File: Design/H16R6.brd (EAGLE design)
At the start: 30 x 34.6 mm, 111 parts, among them IC1 74LVC2T45HK3-7, P1 HEXABIT_17.32, U1 STM32G0B1CEU6N, X1 XTALL_CSTCE8M00G52

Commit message: Edit the logo Add the TVS diode
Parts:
- added D66: BOURNS_CDSOD323-T03SCBOURNS_CDSOD323-T03SC_0_0, HEXABITZ_RCLS:BOURNS_CDSOD323-T03SC_0
- added TRIMBLE-LOGO1: HEXA-LOGO, HEXABITZ_USER_INTERFACE_PARTS:HEXA-LOGO
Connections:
- net GND: now also D66.1
- net VDD: now also D66.2
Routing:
- net GND: track 3.19 -> 4.65 mm
- net VDD: track 23.7 -> 24.2 mm

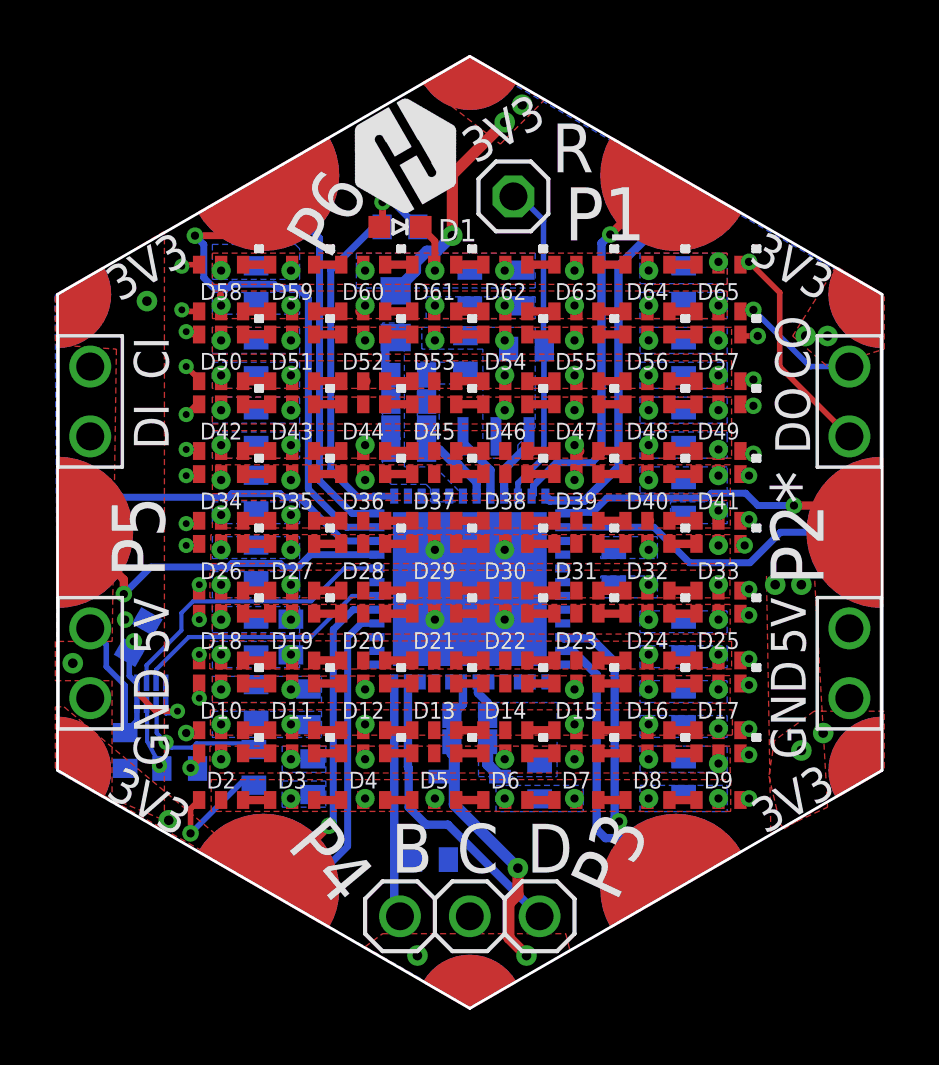
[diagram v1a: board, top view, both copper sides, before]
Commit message: Fix the clearance and soldermask issues Replace the 0603 4.7uF tant cap with ceramic cap in the BOM
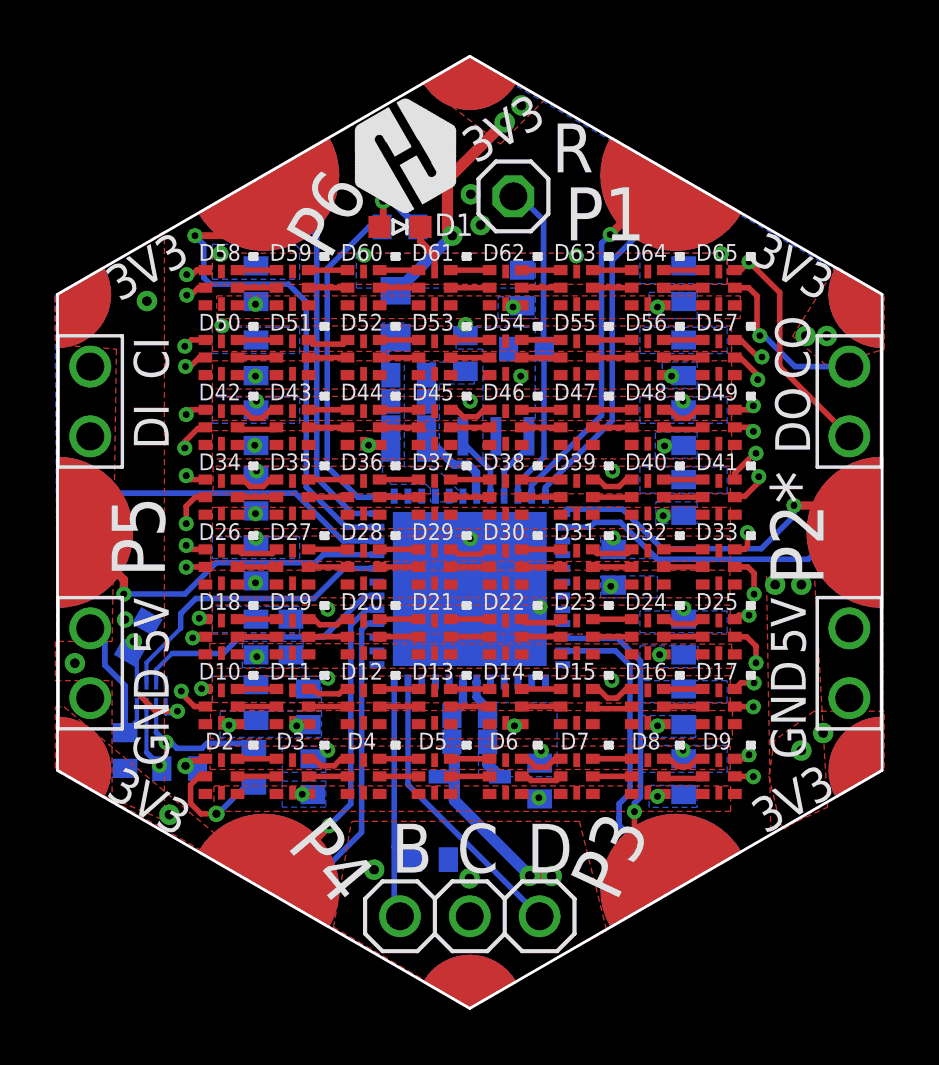
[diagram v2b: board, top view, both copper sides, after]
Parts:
- removed C1: 100nF, HEXABITZ_RCLS:C-0402
- moved SERIAL_IN 27.6 mm to (-13.8, 23.3)
- moved SERIAL_OUT 27.6 mm to (13.8, 23.3)
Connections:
- net +VS: now also D10.VDD1, D11.VDD1, D12.VDD1, D13.VDD1, D14.VDD1, D15.VDD1, D16.VDD1, D17.VDD1, D18.VDD1, D19.VDD1, D2.VDD1, D20.VDD1, D21.VDD1, D22.VDD1, D23.VDD1, D24.VDD1, D25.VDD1, D26.VDD1, D27.VDD1, D28.VDD1, D29.VDD1, D3.VDD1, D30.VDD1, D31.VDD1, D32.VDD1, D33.VDD1, D34.VDD1, D35.VDD1, D36.VDD1, D37.VDD1, D38.VDD1, D39.VDD1, D4.VDD1, D40.VDD1, D41.VDD1, D42.VDD1, D43.VDD1, D44.VDD1, D45.VDD1, D46.VDD1, D47.VDD1, D48.VDD1, D49.VDD1, D5.VDD1, D50.VDD1, D51.VDD1, D52.VDD1, D53.VDD1, D54.VDD1, D55.VDD1, D56.VDD1, D57.VDD1, D58.VDD1, D59.VDD1, D6.VDD1, D60.VDD1, D61.VDD1, D62.VDD1, D63.VDD1, D64.VDD1, D65.VDD1, D7.VDD1, D8.VDD1, D9.VDD1; no longer C1.1
- net CKI: now also SERIAL_IN.1; no longer SERIAL_OUT.1
- net CKO: now also D65.CO, SERIAL_OUT.1; no longer D65.CKO, SERIAL_IN.1
- net GND: no longer C1.2
- net L1_CLK: now also D10.CI, D9.CO; no longer D10.CKI, D9.CKO
- net L1_DATA: now also D10.DI, D9.DO; no longer D10.SDI, D9.SDO
- net L2_CLK: now also D17.CO, D18.CI; no longer D17.CKO, D18.CKI
- net L2_DATA: now also D17.DO, D18.DI; no longer D17.SDO, D18.SDI
- net L3_CLK: now also D25.CO, D26.CI; no longer D25.CKO, D26.CKI
- net L3_DATA: now also D25.DO, D26.DI; no longer D25.SDO, D26.SDI
- net L4_CLK: now also D33.CO, D34.CI; no longer D33.CKO, D34.CKI
- net L4_DATA: now also D33.DO, D34.DI; no longer D33.SDO, D34.SDI
- net L5_CLK: now also D41.CO, D42.CI; no longer D41.CKO, D42.CKI
- net L5_DATA: now also D41.DO, D42.DI; no longer D41.SDO, D42.SDI
- net L6_CLK: now also D49.CO, D50.CI; no longer D49.CKO, D50.CKI
- net L6_DATA: now also D49.DO, D50.DI; no longer D49.SDO, D50.SDI
- net L7_CLK: now also D57.CO, D58.CI; no longer D57.CKO, D58.CKI
- net L7_DATA: now also D57.DO, D58.DI; no longer D57.SDO, D58.SDI
- net N$1: now also D3.DO, D4.DI; no longer D3.SDO, D4.SDI
- net N$10: now also D8.CO, D9.CI; no longer D8.CKO, D9.CKI
- net N$100: now also D45.DO, D46.DI; no longer D45.SDO, D46.SDI
- net N$101: now also D45.CO, D46.CI; no longer D45.CKO, D46.CKI
- net N$102: now also D46.CO, D47.CI; no longer D46.CKO, D47.CKI
- net N$103: now also D46.DO, D47.DI; no longer D46.SDO, D47.SDI
- net N$104: now also D47.CO, D48.CI; no longer D47.CKO, D48.CKI
- net N$105: now also D47.DO, D48.DI; no longer D47.SDO, D48.SDI
- net N$106: now also D12.DO, D13.DI; no longer D12.SDO, D13.SDI
- net N$107: now also D13.DO, D14.DI; no longer D13.SDO, D14.SDI
- net N$108: now also D13.CO, D14.CI; no longer D13.CKO, D14.CKI
- net N$109: now also D14.CO, D15.CI; no longer D14.CKO, D15.CKI
- net N$11: now also D7.CO, D8.CI; no longer D7.CKO, D8.CKI
- net N$110: now also D14.DO, D15.DI; no longer D14.SDO, D15.SDI
- net N$111: now also D15.CO, D16.CI; no longer D15.CKO, D16.CKI
- net N$112: now also D15.DO, D16.DI; no longer D15.SDO, D16.SDI
- net N$113: now also D4.CO, D5.CI; no longer D4.CKO, D5.CKI
- net N$114: now also D4.DO, D5.DI; no longer D4.SDO, D5.SDI
- net N$115: now also D6.CO, D7.CI; no longer D6.CKO, D7.CKI
- net N$116: now also D6.DO, D7.DI; no longer D6.SDO, D7.SDI
- net N$119: now also D2.DI; no longer D2.SDI
- net N$12: now also D7.DO, D8.DI; no longer D7.SDO, D8.SDI
- net N$120: now also D2.CI; no longer D2.CKI
- net N$13: now also D5.CO, D6.CI; no longer D5.CKO, D6.CKI
- net N$14: now also D5.DO, D6.DI; no longer D5.SDO, D6.SDI
- net N$15: now also D16.CO, D17.CI; no longer D16.CKO, D17.CKI
- net N$16: now also D16.DO, D17.DI; no longer D16.SDO, D17.SDI
- net N$17: now also D10.CO, D11.CI; no longer D10.CKO, D11.CKI
- net N$18: now also D10.DO, D11.DI; no longer D10.SDO, D11.SDI
- net N$19: now also D11.CO, D12.CI; no longer D11.CKO, D12.CKI
- net N$2: now also D3.CO, D4.CI; no longer D3.CKO, D4.CKI
- net N$20: now also D11.DO, D12.DI; no longer D11.SDO, D12.SDI
- net N$21: now also D12.CO, D13.CI; no longer D12.CKO, D13.CKI
- net N$22: now also D18.CO, D19.CI; no longer D18.CKO, D19.CKI
- net N$23: now also D18.DO, D19.DI; no longer D18.SDO, D19.SDI
- net N$24: now also D19.CO, D20.CI; no longer D19.CKO, D20.CKI
- net N$25: now also D19.DO, D20.DI; no longer D19.SDO, D20.SDI
- net N$26: now also D20.CO, D21.CI; no longer D20.CKO, D21.CKI
- net N$27: now also D20.DO, D21.DI; no longer D20.SDO, D21.SDI
- net N$28: now also D21.CO, D22.CI; no longer D21.CKO, D22.CKI
- net N$29: now also D21.DO, D22.DI; no longer D21.SDO, D22.SDI
- net N$30: now also D22.CO, D23.CI; no longer D22.CKO, D23.CKI
- net N$31: now also D22.DO, D23.DI; no longer D22.SDO, D23.SDI
- net N$32: now also D23.CO, D24.CI; no longer D23.CKO, D24.CKI
- net N$33: now also D23.DO, D24.DI; no longer D23.SDO, D24.SDI
- net N$34: now also D24.CO, D25.CI; no longer D24.CKO, D25.CKI
- net N$35: now also D24.DO, D25.DI; no longer D24.SDO, D25.SDI
- net N$36: now also D26.CO, D27.CI; no longer D26.CKO, D27.CKI
- net N$37: now also D26.DO, D27.DI; no longer D26.SDO, D27.SDI
- net N$38: now also D27.CO, D28.CI; no longer D27.CKO, D28.CKI
- net N$39: now also D27.DO, D28.DI; no longer D27.SDO, D28.SDI
- net N$40: now also D28.CO, D29.CI; no longer D28.CKO, D29.CKI
- net N$41: now also D28.DO, D29.DI; no longer D28.SDO, D29.SDI
- net N$42: now also D29.CO, D30.CI; no longer D29.CKO, D30.CKI
- net N$43: now also D29.DO, D30.DI; no longer D29.SDO, D30.SDI
- net N$44: now also D31.CO, D32.CI; no longer D31.CKO, D32.CKI
- net N$45: now also D31.DO, D32.DI; no longer D31.SDO, D32.SDI
- net N$46: now also D30.CO, D31.CI; no longer D30.CKO, D31.CKI
- net N$47: now also D30.DO, D31.DI; no longer D30.SDO, D31.SDI
- net N$48: now also D32.CO, D33.CI; no longer D32.CKO, D33.CKI
- net N$49: now also D32.DO, D33.DI; no longer D32.SDO, D33.SDI
- net N$50: now also D34.CO, D35.CI; no longer D34.CKO, D35.CKI
- net N$51: now also D34.DO, D35.DI; no longer D34.SDO, D35.SDI
- net N$52: now also D35.CO, D36.CI; no longer D35.CKO, D36.CKI
- net N$53: now also D35.DO, D36.DI; no longer D35.SDO, D36.SDI
- net N$54: now also D36.CO, D37.CI; no longer D36.CKO, D37.CKI
- net N$55: now also D36.DO, D37.DI; no longer D36.SDO, D37.SDI
- net N$56: now also D37.CO, D38.CI; no longer D37.CKO, D38.CKI
- net N$57: now also D37.DO, D38.DI; no longer D37.SDO, D38.SDI
- net N$58: now also D38.CO, D39.CI; no longer D38.CKO, D39.CKI
- net N$59: now also D38.DO, D39.DI; no longer D38.SDO, D39.SDI
- net N$60: now also D40.CO, D41.CI; no longer D40.CKO, D41.CKI
- net N$61: now also D40.DO, D41.DI; no longer D40.SDO, D41.SDI
- net N$62: now also D39.CO, D40.CI; no longer D39.CKO, D40.CKI
- net N$63: now also D39.DO, D40.DI; no longer D39.SDO, D40.SDI
- net N$64: now also D48.CO, D49.CI; no longer D48.CKO, D49.CKI
- net N$65: now also D48.DO, D49.DI; no longer D48.SDO, D49.SDI
- net N$66: now also D56.CO, D57.CI; no longer D56.CKO, D57.CKI
- net N$67: now also D56.DO, D57.DI; no longer D56.SDO, D57.SDI
- net N$68: now also D64.CO, D65.CI; no longer D64.CKO, D65.CKI
- net N$69: now also D64.DO, D65.DI; no longer D64.SDO, D65.SDI
- net N$7: now also D2.DO, D3.DI; no longer D2.SDO, D3.SDI
- net N$70: now also D55.DO, D56.DI; no longer D55.SDO, D56.SDI
- net N$71: now also D55.CO, D56.CI; no longer D55.CKO, D56.CKI
- net N$72: now also D63.CO, D64.CI; no longer D63.CKO, D64.CKI
- net N$73: now also D63.DO, D64.DI; no longer D63.SDO, D64.SDI
- net N$74: now also D54.CO, D55.CI; no longer D54.CKO, D55.CKI
- net N$75: now also D54.DO, D55.DI; no longer D54.SDO, D55.SDI
- net N$76: now also D62.CO, D63.CI; no longer D62.CKO, D63.CKI
- net N$77: now also D62.DO, D63.DI; no longer D62.SDO, D63.SDI
- net N$78: now also D61.DO, D62.DI; no longer D61.SDO, D62.SDI
- net N$79: now also D61.CO, D62.CI; no longer D61.CKO, D62.CKI
- net N$8: now also D2.CO, D3.CI; no longer D2.CKO, D3.CKI
- net N$80: now also D60.CO, D61.CI; no longer D60.CKO, D61.CKI
- net N$81: now also D60.DO, D61.DI; no longer D60.SDO, D61.SDI
- net N$82: now also D59.CO, D60.CI; no longer D59.CKO, D60.CKI
- net N$83: now also D59.DO, D60.DI; no longer D59.SDO, D60.SDI
- net N$84: now also D58.DO, D59.DI; no longer D58.SDO, D59.SDI
- net N$85: now also D58.CO, D59.CI; no longer D58.CKO, D59.CKI
- net N$86: now also D53.DO, D54.DI; no longer D53.SDO, D54.SDI
- net N$87: now also D53.CO, D54.CI; no longer D53.CKO, D54.CKI
- net N$88: now also D51.CO, D52.CI; no longer D51.CKO, D52.CKI
- net N$89: now also D51.DO, D52.DI; no longer D51.SDO, D52.SDI
- net N$9: now also D8.DO, D9.DI; no longer D8.SDO, D9.SDI
- net N$90: now also D52.DO, D53.DI; no longer D52.SDO, D53.SDI
- net N$91: now also D52.CO, D53.CI; no longer D52.CKO, D53.CKI
- net N$92: now also D50.DO, D51.DI; no longer D50.SDO, D51.SDI
- net N$93: now also D50.CO, D51.CI; no longer D50.CKO, D51.CKI
- net N$94: now also D42.CO, D43.CI; no longer D42.CKO, D43.CKI
- net N$95: now also D42.DO, D43.DI; no longer D42.SDO, D43.SDI
- net N$96: now also D43.CO, D44.CI; no longer D43.CKO, D44.CKI
- net N$97: now also D43.DO, D44.DI; no longer D43.SDO, D44.SDI
- net N$98: now also D44.CO, D45.CI; no longer D44.CKO, D45.CKI
- net N$99: now also D44.DO, D45.DI; no longer D44.SDO, D45.SDI
- net SDI: now also SERIAL_IN.2; no longer SERIAL_OUT.2
- net SDO: now also D65.DO, SERIAL_OUT.2; no longer D65.SDO, SERIAL_IN.2
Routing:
- net L3_CLK: track 21.8 -> 24.4 mm
- net L1_CLK: track 22.5 -> 24.8 mm
- net L4_CLK: track 22.5 -> 24.7 mm
- net VDD: track 24.2 -> 22.0 mm
- net +VS: track 9.67 -> 11.8 mm, vias 44 -> 22
- net L5_CLK: track 22.6 -> 24.5 mm
- net L2_CLK: track 21.7 -> 23.0 mm
- net CKO: track 4.84 -> 6.14 mm
- net USART4_RX: track 14.0 -> 12.9 mm
- net USART2_TX: track 11.8 -> 12.9 mm
- net L1_DATA: track 21.7 -> 22.7 mm
- net L4_DATA: track 22.0 -> 23.0 mm
- net USART3_RX: track 10.4 -> 11.3 mm
- net USART3_TX: track 10.7 -> 11.5 mm
- net USART4_TX: track 14.1 -> 13.4 mm
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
